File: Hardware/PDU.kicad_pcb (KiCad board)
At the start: 4 copper layers, 65.5 x 50 mm, 150 parts, among them IC1 SiC437AED-T1-GE3, J1 Conn_01x03_MountingPin, J10 USB_C_Receptacle_USB2.0, J2 Conn_01x04_Male, J3 XT60PW-M, J4 XT60PW-M, J5 Conn_01x02_Male, J6 Conn_01x08_Male, J7 FAN, J8 XT60PW-F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

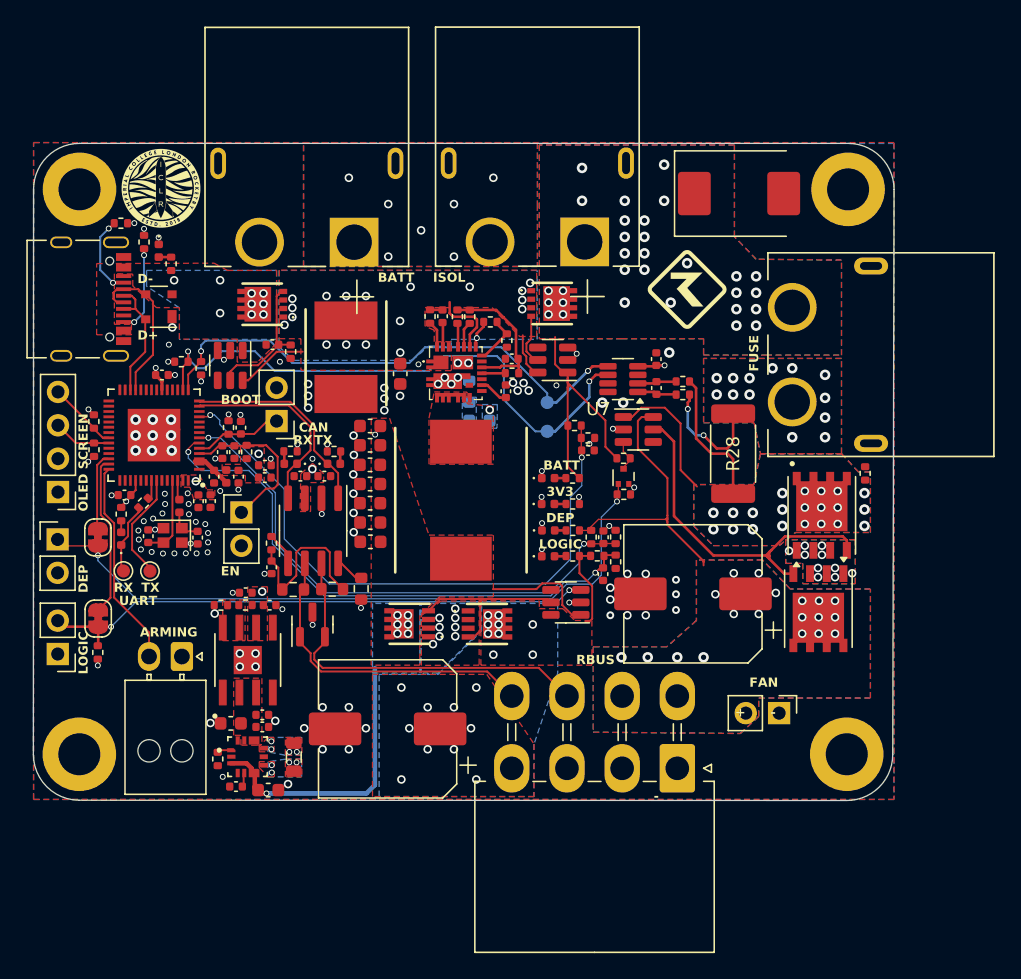
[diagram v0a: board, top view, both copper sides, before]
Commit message: feat: Via and track sizes for eurocircuits
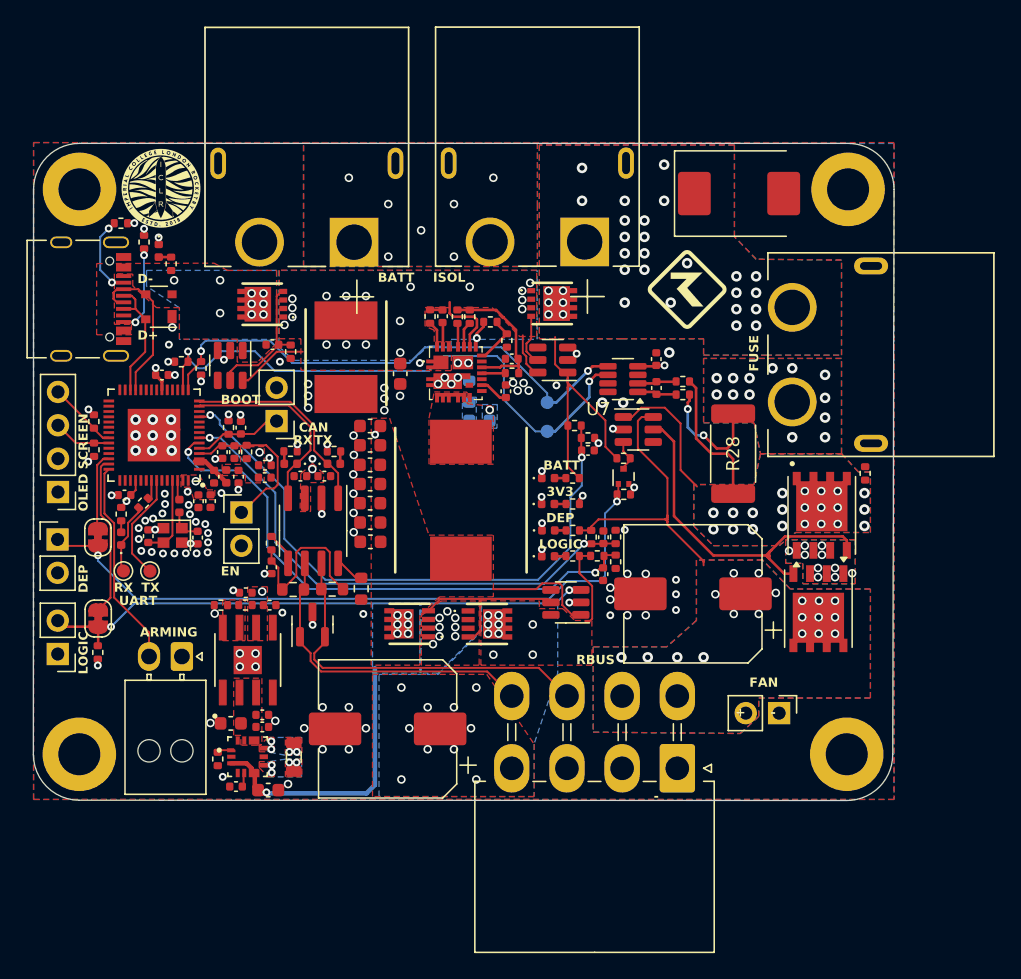
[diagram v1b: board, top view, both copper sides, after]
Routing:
- net /DepVoltage: track 41.0 -> 39.8 mm
- net /BattVoltage: track 47.4 -> 46.6 mm

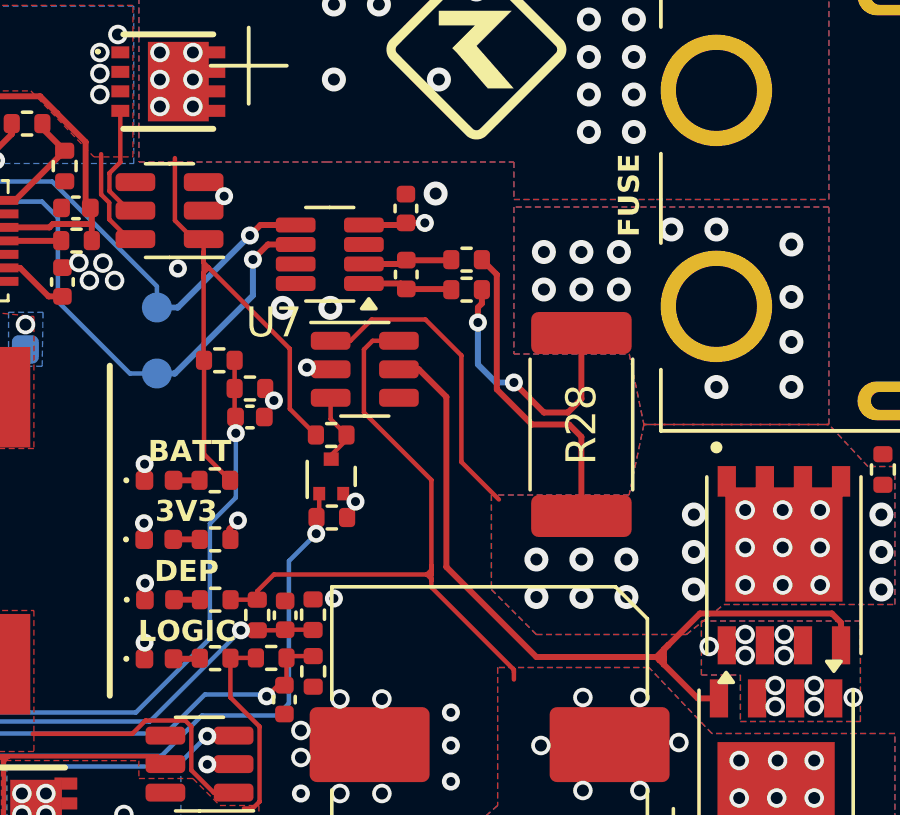
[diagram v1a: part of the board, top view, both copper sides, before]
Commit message: feat: GND and 3V3 plane solid + current sense GND exclusion
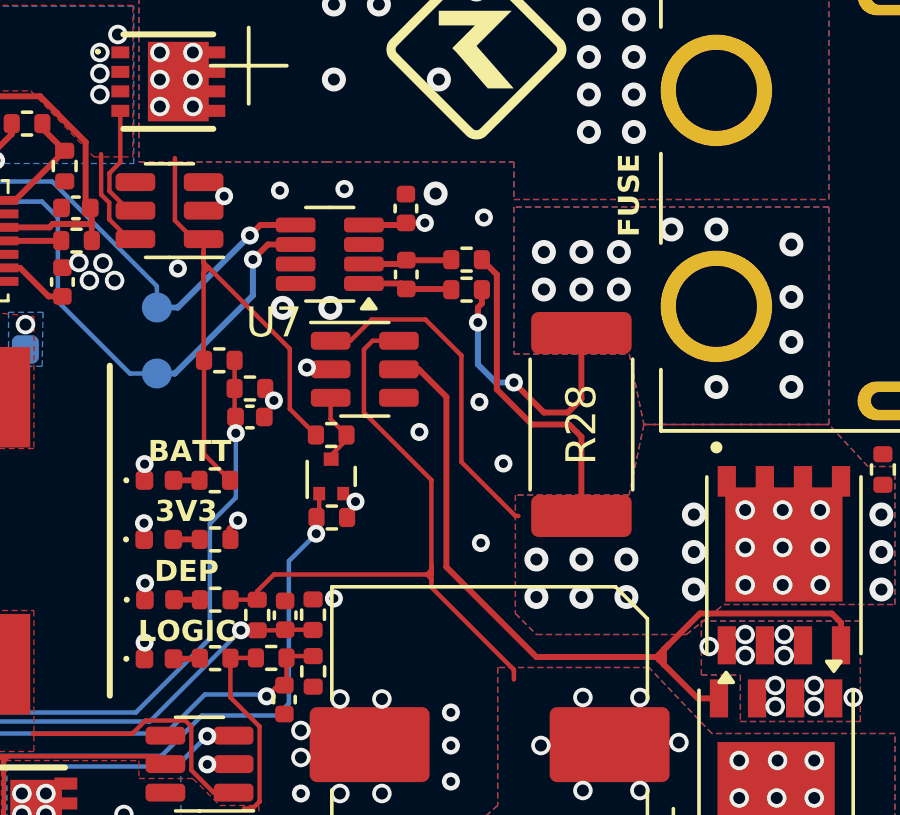
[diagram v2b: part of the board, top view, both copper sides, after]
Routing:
- net /Switches+RBUS/Fuse_OUT: track 21.1 -> 22.0 mm
- net GND: vias 116 -> 123
- removed copper zone on In1.Cu, net +12V
- removed copper zone on In2.Cu, net +12V
- removed copper zone on In1.Cu, net /Switches+RBUS/Fuse_OUT
- removed copper zone on In2.Cu, net /Switches+RBUS/Fuse_OUT
- removed copper zone on In1.Cu, net Net-(J6-Pin_5)
- removed copper zone on In2.Cu, net Net-(J6-Pin_5)
- removed copper zone on In1.Cu, net Net-(J8-Pad1)
- removed copper zone on In2.Cu, net Net-(J8-Pad1)
- removed copper zone on In1.Cu, net Net-(Q3-Pad1)
- removed copper zone on In2.Cu, net Net-(Q3-Pad1)

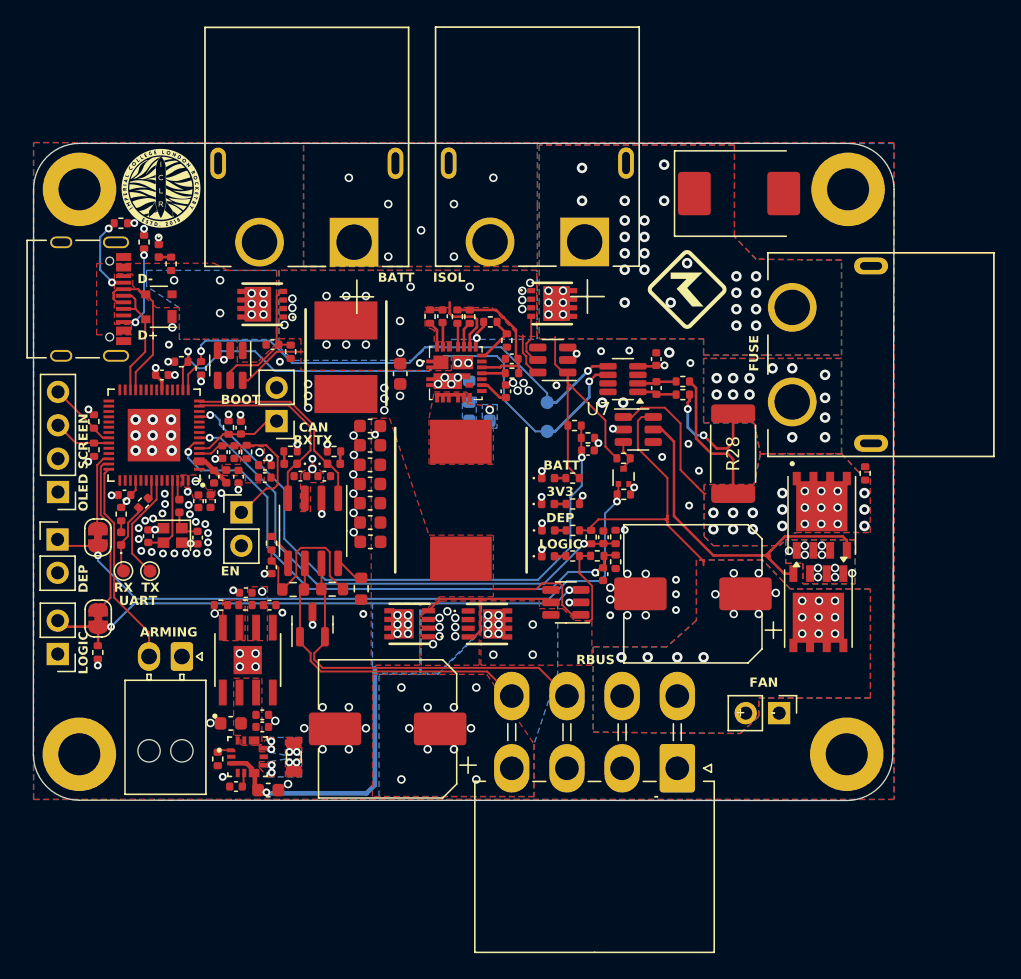
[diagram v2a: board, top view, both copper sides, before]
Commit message: feat: Via size for eurocircuits, adjusted inner layer USBC
fixing stuff for eurocircuits
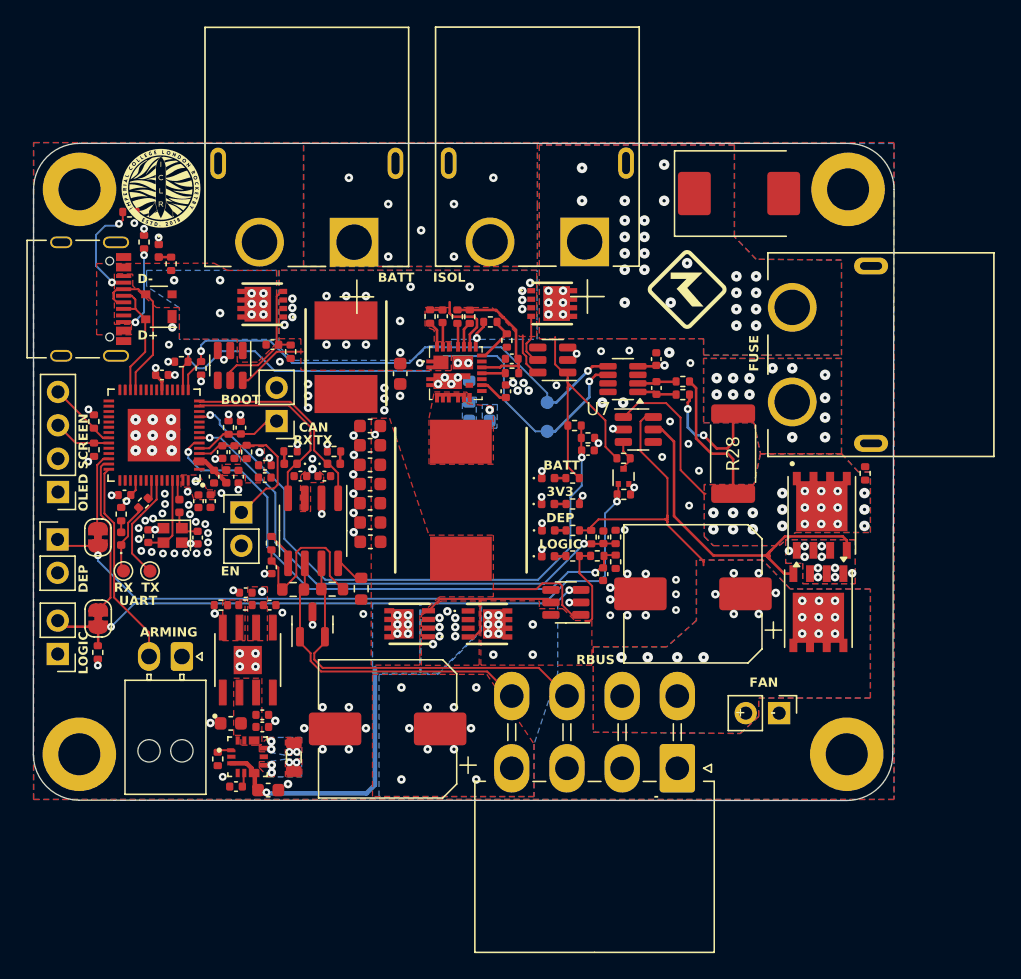
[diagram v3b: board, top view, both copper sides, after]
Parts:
- moved R36 1.08 mm to (120.8, 75.7)
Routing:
- net Net-(J10-CC1): track 6.23 -> 8.14 mm
- net /Switches+RBUS/Fuse_OUT: track 22.0 -> 22.5 mm
- net GND: vias 123 -> 124
- added copper zone on In2.Cu, net GND
